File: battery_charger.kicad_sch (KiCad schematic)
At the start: 44 parts, among them Q3 NMOS, Q4 NMOS, Q6 NMOS, Q7 NMOS, Q8 NMOS, U1 BQ24725A

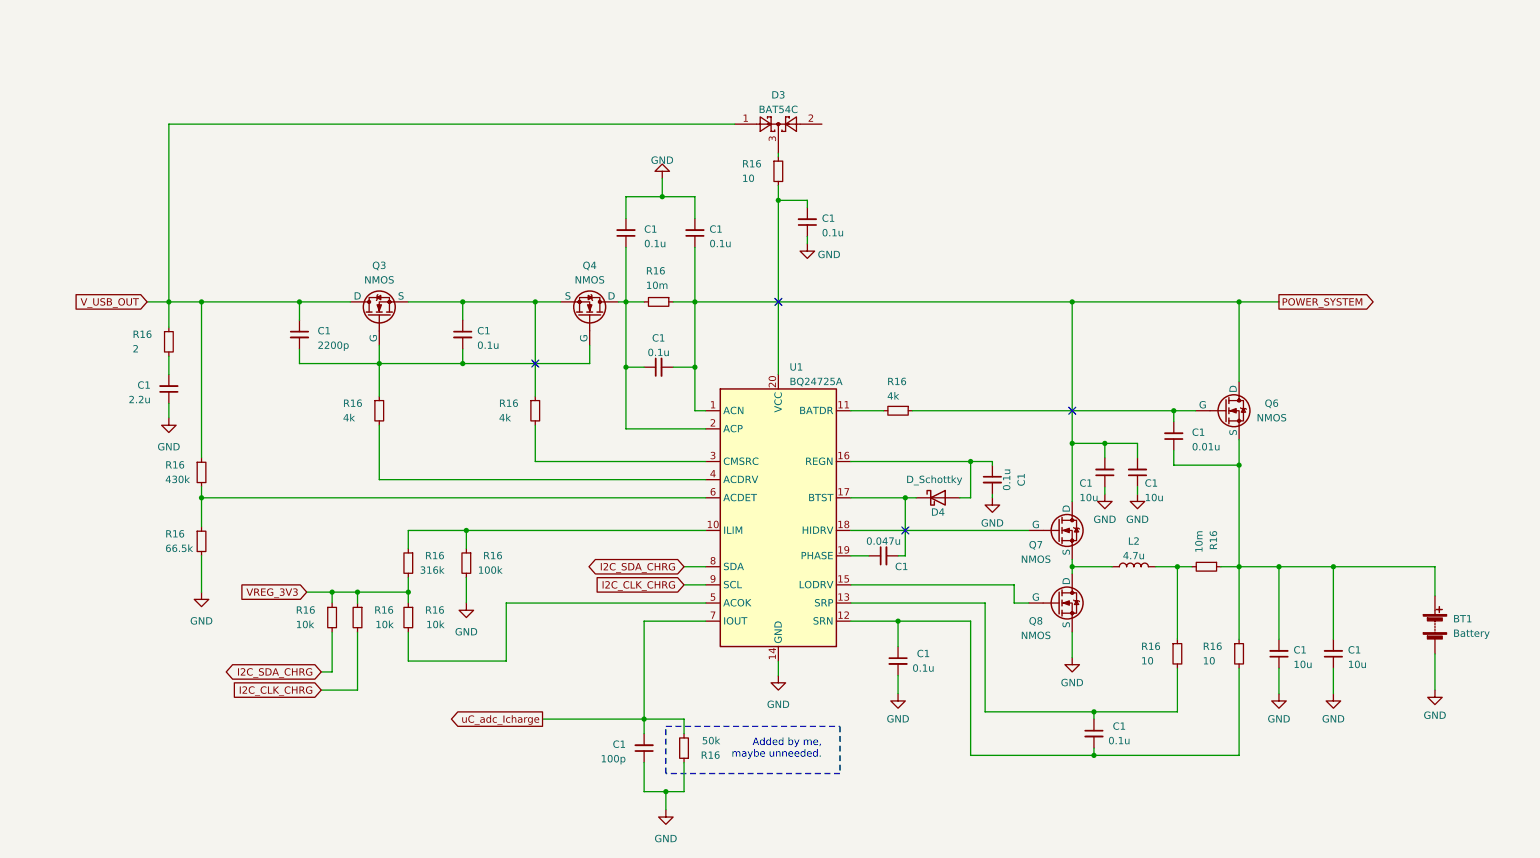
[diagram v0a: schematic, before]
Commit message: Added microcontroller stage. Need to fix the supply routing to power from battery.
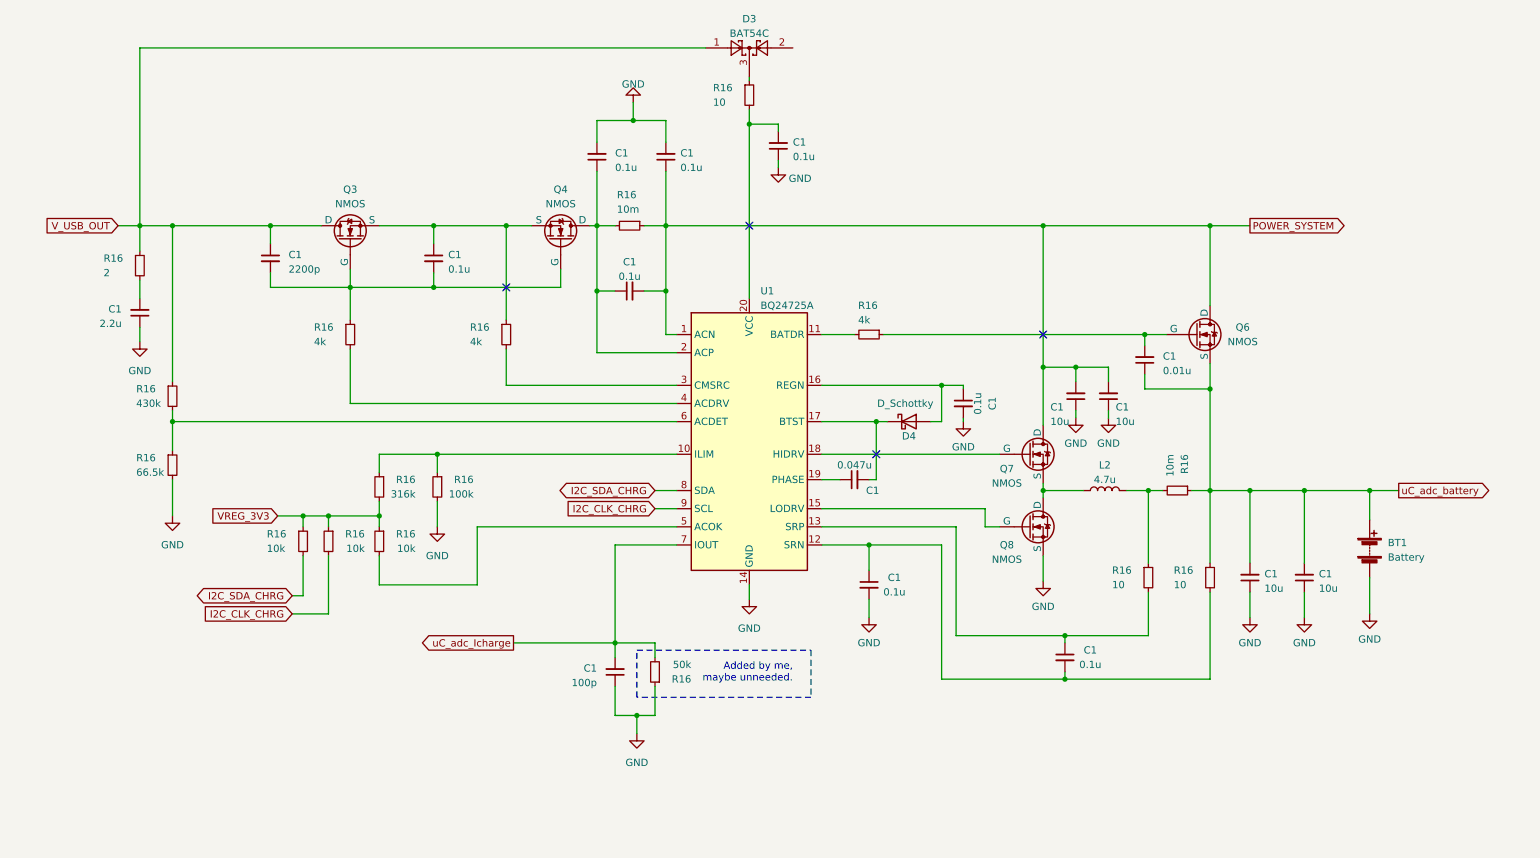
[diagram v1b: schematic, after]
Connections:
- net uC_adc_battery: now reaches BT1.1 (+), C1.1, C1.2, C1.2, Q6.3 (S), R16.1, R16.1
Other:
- moved on the sheet: BT1, C1, D3, D4, L2, Q3, Q4, Q6, Q7, Q8, R16, U1

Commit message: Schematic completed. Started routing.
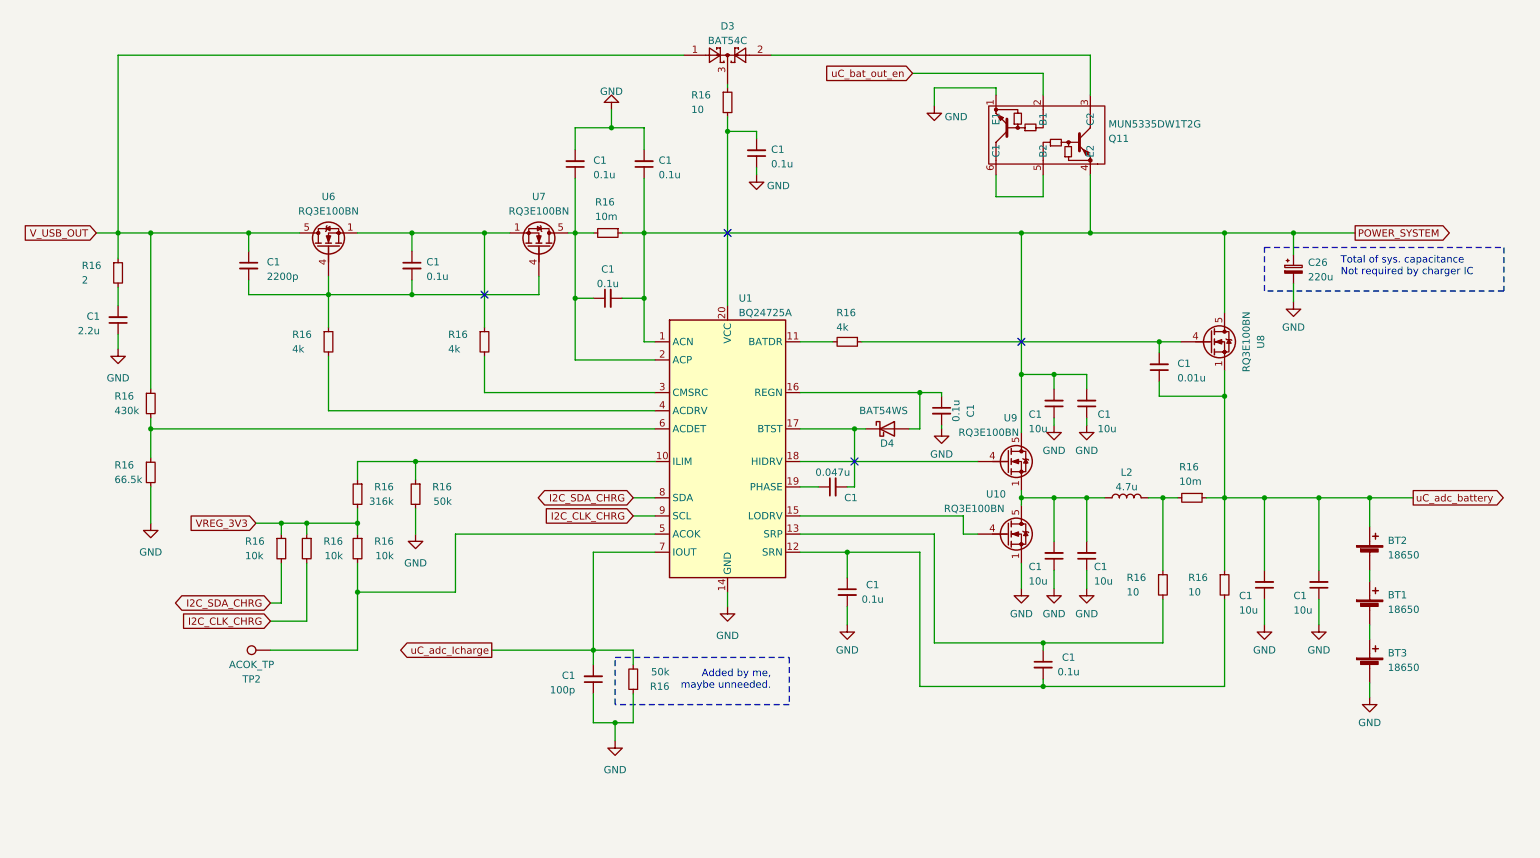
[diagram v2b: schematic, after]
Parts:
- removed BT1: Battery, symbol Device:Battery
- removed C1 (x3): 10u, Capacitor_SMD:C_0805_2012Metric_Pad1.18x1.45mm_HandSolder, symbol Device:C_Small
- removed Q3, Q4, Q6, Q7, Q8: NMOS, symbol Simulation_SPICE:NMOS
- added BT1, BT2, BT3: 18650, User_Battery:Battery_18650, symbol Device:Battery_Cell
- added C1 (x5): 10u, Capacitor_SMD:C_1206_3216Metric_Pad1.33x1.80mm_HandSolder, symbol Device:C_Small
- added C26: 220u, Capacitor_SMD:CP_Elec_8x10, symbol Device:C_Polarized_Small
- added Q11: MUN5335DW1T2G, Package_TO_SOT_SMD:SOT-363_SC-70-6_Handsoldering, symbol BRTs:MUN5335DW1T2G
- added TP2: ACOK_TP, TestPoint:TestPoint_Pad_2.5x2.5mm, symbol Connector:TestPoint
- added U10, U6, U7, U8, U9: RQ3E100BN, User_Mosfet:HSMT8, symbol User_MOSFET:RQ3E100BN
- C1: footprint Capacitor_SMD:C_0805_2012Metric_Pad1.18x1.45mm_HandSolder -> Capacitor_SMD:C_1206_3216Metric_Pad1.33x1.80mm_HandSolder; Price (none) -> 0.09; Vendor (none) -> https://www.mouser.com/ProductDetail/Samsung-Electro-Mechan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
- D4: value D_Schottky -> BAT54WS; footprint (none) -> Diode_SMD:D_SOD-323_HandSoldering; Price (none) -> 0.08; Vendor (none) -> https://www.mouser.com/ProductDetail/Diodes-Incorporated/BA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
- L2: footprint (none) -> Inductor_SMD:L_Bourns_SRN8040TA; Price (none) -> 0.38; Vendor (none) -> https://www.mouser.com/ProductDetail/Bourns/SRN8040TA-4R7M?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
- R16: footprint Resistor_SMD:R_0805_2012Metric_Pad1.20x1.40mm_HandSolder -> Resistor_SMD:R_1206_3216Metric_Pad1.30x1.75mm_HandSolder; Price (none) -> 0.15; Vendor (none) -> https://www.mouser.com/ProductDetail/Bussmann-Eaton/MFL1206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
- R16: value 100k -> 50k
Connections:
- net GND: now also BT3.2 (-), C1.1, C1.1, C1.1, C1.1, C1.1, C26.2, Q11.1 (E1), U10.1, U10.2, U10.3
- net POWER_SYSTEM: now also C1.2, C26.1, Q11.4 (E2), U8.5, U9.5
- net V_USB_OUT: now also U6.5
- net uC_adc_battery: now also BT2.1 (+), C1.2, C1.2, U8.1, U8.2, U8.3
- net at C1.1, C1.1, R16.2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: now also U7.5
- net at R16.2, U1.5 (ACOK): now also TP2.1
- net at U1.15 (LODRV): now also U10.4
- net at U1.18 (HIDRV): now also U9.4
- net at C1.2, R16.1: now also U8.4
- net at C1.2, C1.2, R16.1: now also U6.4, U7.4
- net at C1.1, R16.1: now also U6.1, U6.2, U6.3, U7.1, U7.2, U7.3
- net at D3.2: now also Q11.3 (C2)
- net at L2.1: now also C1.2, C1.2, U10.5, U9.1, U9.2, U9.3
- new net: Q11.5 (B2), Q11.6 (C1)
- new net: BT1.2 (-), BT3.1 (+)
- new net: BT1.1 (+), BT2.2 (-)
- new net uC_bat_out_en: Q11.2 (B1)
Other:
- note added: "Total of sys. capacitance Not required by charger IC"
- moved on the sheet: C1, D3, D4, L2, R16, U1

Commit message: Re-reouting the USB C CCX lines
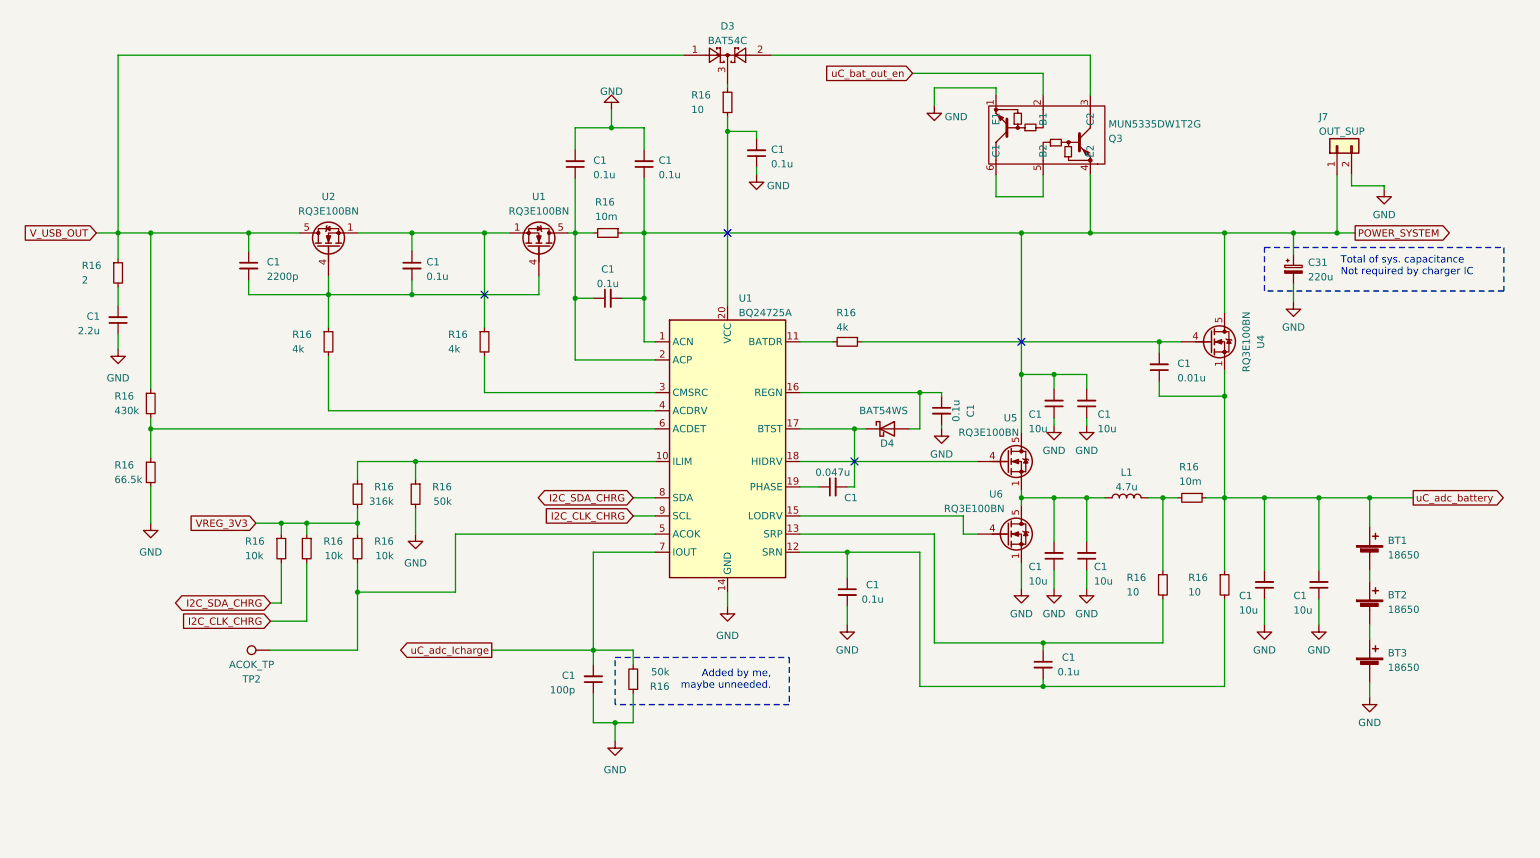
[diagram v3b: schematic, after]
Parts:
- added J7: OUT_SUP, Connector_PinHeader_2.54mm:PinHeader_1x02_P2.54mm_Vertical, symbol Connector_Generic:Conn_01x02
- renumbered C26 to C31, L2 to L1, Q11 to Q3, U7 to U1, U6 to U2, U8 to U4, U9 to U5, U10 to U6
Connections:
- net GND: now also J7.2 (Pin_2)
- net POWER_SYSTEM: now also J7.1 (Pin_1)
- net uC_adc_battery: now also BT1.1 (+); no longer BT2.1 (+)
- net at BT3.1 (+): now also BT2.2 (-); no longer BT1.2 (-)
- new net: BT1.2 (-), BT2.1 (+)
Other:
- moved on the sheet: BT1, BT2
